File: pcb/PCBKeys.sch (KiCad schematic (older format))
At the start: 0 parts

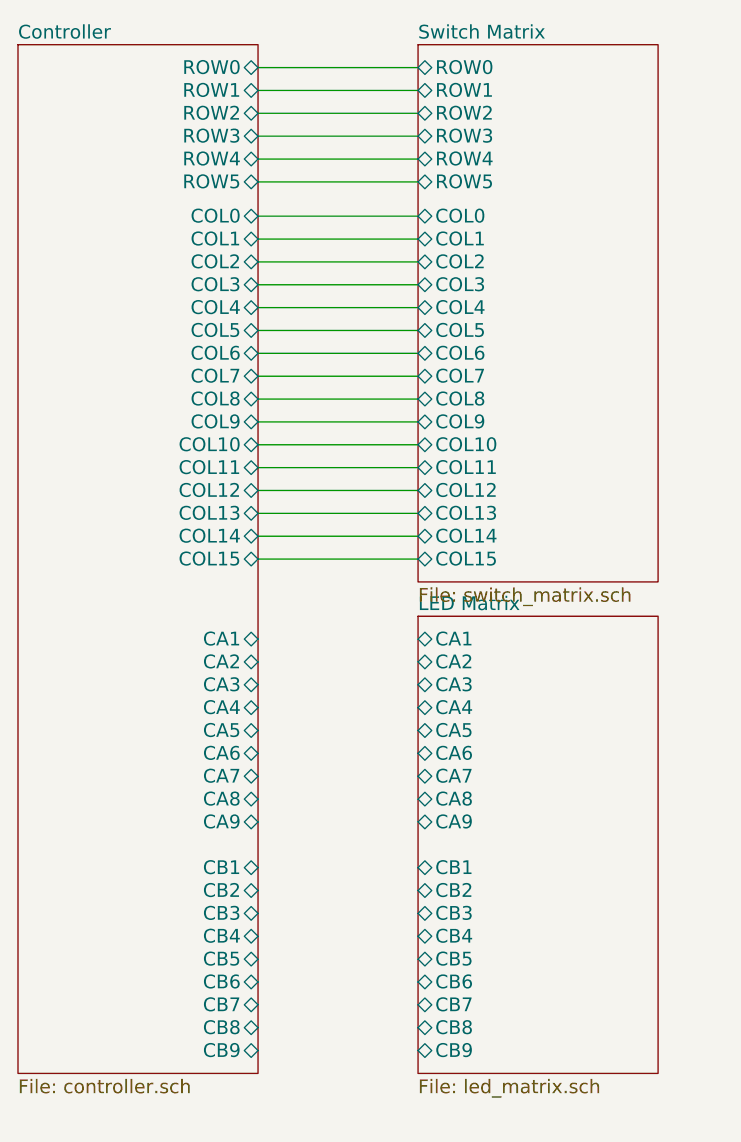
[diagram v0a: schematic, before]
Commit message: changes in schematic
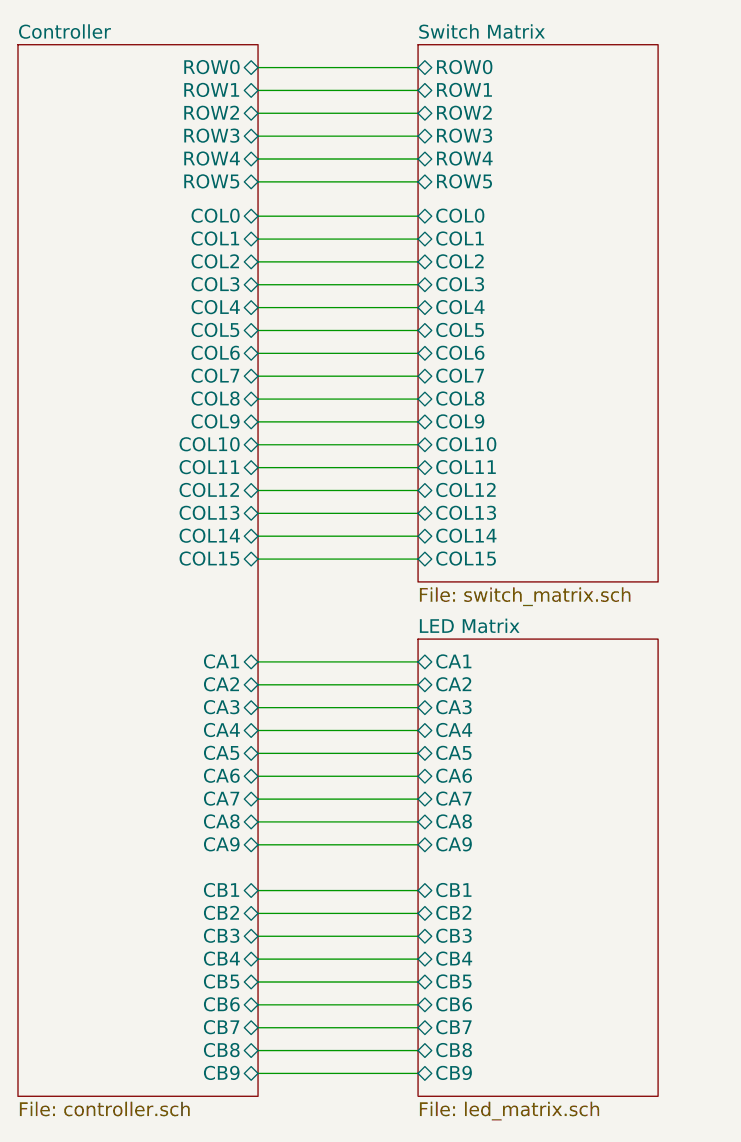
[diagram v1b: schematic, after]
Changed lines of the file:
@@
 $EndDescr
 $Sheet
-S 1150 1350 1050 4500
+S 1150 1350 1050 4600
 U 5AB55C58
 F0 "Controller" 60
@@
 F22 "ROW0" B R 2200 1450 60
 F23 "COL15" B R 2200 3600 60
-F24 "CA1" B R 2200 3950 60
-F25 "CA2" B R 2200 4050 60
-F26 "CA3" B R 2200 4150 60
-F27 "CA4" B R 2200 4250 60
-F28 "CA5" B R 2200 4350 60
-F29 "CA6" B R 2200 4450 60
-F30 "CA7" B R 2200 4550 60
-F31 "CA8" B R 2200 4650 60
-F32 "CA9" B R 2200 4750 60
-F33 "CB1" B R 2200 4950 60
-F34 "CB2" B R 2200 5050 60
-F35 "CB3" B R 2200 5150 60
-F36 "CB4" B R 2200 5250 60
-F37 "CB5" B R 2200 5350 60
-F38 "CB6" B R 2200 5450 60
-F39 "CB7" B R 2200 5550 60
-F40 "CB8" B R 2200 5650 60
-F41 "CB9" B R 2200 5750 60
+F24 "CA1" B R 2200 4050 60
+F25 "CA2" B R 2200 4150 60
+F26 "CA3" B R 2200 4250 60
+F27 "CA4" B R 2200 4350 60
+F28 "CA5" B R 2200 4450 60
+F29 "CA6" B R 2200 4550 60
+F30 "CA7" B R 2200 4650 60
+F31 "CA8" B R 2200 4750 60
+F32 "CA9" B R 2200 4850 60
+F33 "CB1" B R 2200 5050 60
+F34 "CB2" B R 2200 5150 60
+F35 "CB3" B R 2200 5250 60
+F36 "CB4" B R 2200 5350 60
+F37 "CB5" B R 2200 5450 60
+F38 "CB6" B R 2200 5550 60
+F39 "CB7" B R 2200 5650 60
+F40 "CB8" B R 2200 5750 60
+F41 "CB9" B R 2200 5850 60
 $EndSheet
 $Sheet
@@
 	2200 3500 2900 3500
 $Sheet
-S 2900 3850 1050 2000
+S 2900 3950 1050 2000
 U 5AB7A2C1
 F0 "LED Matrix" 60
 F1 "led_matrix.sch" 60
-F2 "CA1" B L 2900 3950 60
-F3 "CA2" B L 2900 4050 60
-F4 "CA3" B L 2900 4150 60
-F5 "CA4" B L 2900 4250 60
-F6 "CA5" B L 2900 4350 60
-F7 "CA6" B L 2900 4450 60
-F8 "CA7" B L 2900 4550 60
-F9 "CA8" B L 2900 4650 60
-F10 "CA9" B L 2900 4750 60
-F11 "CB1" B L 2900 4950 60
-F12 "CB2" B L 2900 5050 60
-F13 "CB3" B L 2900 5150 60
-F14 "CB4" B L 2900 5250 60
-F15 "CB5" B L 2900 5350 60
-F16 "CB6" B L 2900 5450 60
-F17 "CB7" B L 2900 5550 60
-F18 "CB8" B L 2900 5650 60
-F19 "CB9" B L 2900 5750 60
+F2 "CA1" B L 2900 4050 60
+F3 "CA2" B L 2900 4150 60
+F4 "CA3" B L 2900 4250 60
+F5 "CA4" B L 2900 4350 60
+F6 "CA5" B L 2900 4450 60
+F7 "CA6" B L 2900 4550 60
+F8 "CA7" B L 2900 4650 60
+F9 "CA8" B L 2900 4750 60
+F10 "CA9" B L 2900 4850 60
+F11 "CB1" B L 2900 5050 60
+F12 "CB2" B L 2900 5150 60
+F13 "CB3" B L 2900 5250 60
+F14 "CB4" B L 2900 5350 60
+F15 "CB5" B L 2900 5450 60
+F16 "CB6" B L 2900 5550 60
+F17 "CB7" B L 2900 5650 60
+F18 "CB8" B L 2900 5750 60
+F19 "CB9" B L 2900 5850 60
 $EndSheet
 Wire Wire Line
 	2200 3600 2900 3600
+Wire Wire Line
+	2200 4050 2900 4050
+Wire Wire Line
+	2200 4150 2900 4150
+Wire Wire Line
+	2200 4250 2900 4250
+Wire Wire Line
+	2200 4350 2900 4350
+Wire Wire Line
+	2200 4450 2900 4450
+Wire Wire Line
+	2200 4550 2900 4550
+Wire Wire Line
+	2200 4650 2900 4650
+Wire Wire Line
+	2200 4750 2900 4750
+Wire Wire Line
+	2200 4850 2900 4850
+Wire Wire Line
+	2200 5050 2900 5050
+Wire Wire Line
+	2200 5150 2900 5150
+Wire Wire Line
+	2200 5250 2900 5250
+Wire Wire Line
+	2200 5350 2900 5350
+Wire Wire Line
+	2200 5450 2900 5450
+Wire Wire Line
+	2200 5550 2900 5550
+Wire Wire Line
+	2200 5650 2900 5650
+Wire Wire Line
+	2200 5750 2900 5750
+Wire Wire Line
+	2200 5850 2900 5850
 $EndSCHEMATC
